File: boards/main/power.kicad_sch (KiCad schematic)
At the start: 20 parts, among them Q1 DMG3415U, U3 RT9080-33GJ5, U4 MCP73831T-2ACI_OT, U5 MAX17048G_T10

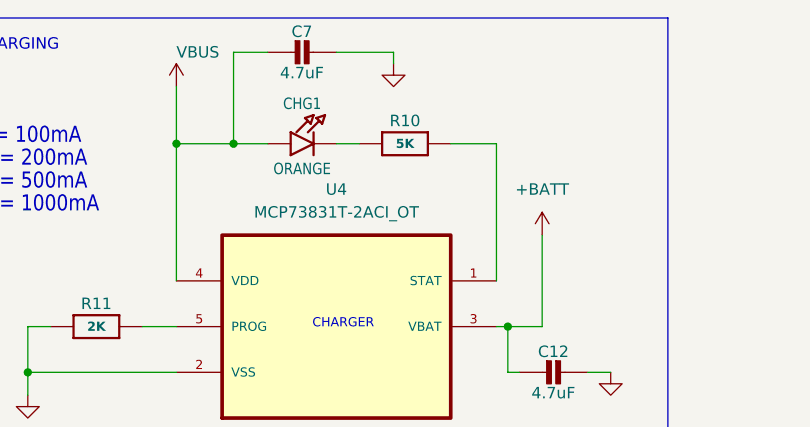
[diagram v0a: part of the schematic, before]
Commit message: Board migrations. Move to newer LED and IMU
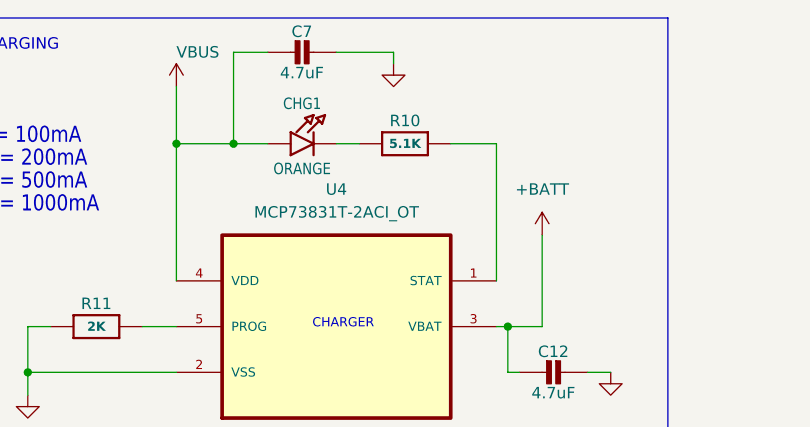
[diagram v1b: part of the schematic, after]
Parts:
- BATT1: DigiKey_PN (none) -> 455-S2B-PH-SM4-TBCT-ND; MPN S2B-PH-SM4-TB(LF)(SN) -> S2B-PH-SM4-TB; Manufacturer (none) -> JST Sales America Inc.
- C10, C14: Dielectric (none) -> X7R; DigiKey_PN (none) -> 1276-6844-1-ND; MPN 0402B104K160HI -> CL05B104KO5VPNC; Manufacturer (none) -> Samsung Electro-Mechanics; Voltage (none) -> 16V
- C11, C13, C8, C9: Dielectric (none) -> X5R; DigiKey_PN (none) -> 1276-6456-1-ND; Manufacturer (none) -> Samsung Electro-Mechanics; Voltage (none) -> 10V
- C12, C7: Dielectric (none) -> X5R; DigiKey_PN (none) -> 1276-1482-1-ND; MPN C0402X5R475M100NTC -> CL05A475MP5NRNC; Manufacturer (none) -> Samsung Electro-Mechanics; Voltage (none) -> 10V
- CHG1: DigiKey_PN (none) -> 160-1447-1-ND; Manufacturer (none) -> Lite-On Inc.; Sourcing_Note (none) -> Value field says ORANGE but LTST-C191KRKT is a RED 631nm LE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
- D1: DigiKey_PN (none) -> MBR0540TPMSCT-ND; MPN MBR0540 -> MBR0540-TP; Manufacturer (none) -> MCC (Micro Commercial Components)
- ONOFF1: DigiKey_PN (none) -> 455-1564-1-ND; Manufacturer (none) -> JST Sales America Inc.
- Q1: DigiKey_PN (none) -> DMG3415UDICT-ND; Manufacturer (none) -> Diodes Incorporated
- R10: value 5K -> 5.1K; DigiKey_PN (none) -> 311-5.10KHRCT-ND; MPN RT0603BRE075KL -> RC0603FR-075K1L; Manufacturer (none) -> YAGEO; Tolerance (none) -> 1%
- R11, R12, R9: Manufacturer (none) -> YAGEO; Tolerance (none) -> 1%
- U3: DigiKey_PN (none) -> 1028-1509-1-ND; Manufacturer (none) -> Richtek USA Inc.
- U4: DigiKey_PN (none) -> MCP73831T-2ACI/OTCT-ND; Manufacturer (none) -> Microchip Technology
- U5: DigiKey_PN (none) -> MAX17048G+T10CT-ND; Manufacturer (none) -> Analog Devices Inc./Maxim Integrated; Sourcing_Note (none) -> Operating range is -20C to +70C, the narrowest of any part 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
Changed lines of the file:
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@@
 			)
 		)
-		(property "MPN" "0402B104K160HI"
+		(property "MPN" "CL05B104KO5VPNC"
 			(at 86.36 101.6 90)
 			(hide yes)
@@
 			)
 		)
+    (property "Manufacturer" "Samsung Electro-Mechanics" (at 86.36 101.6 0)
+      (effects (font (size 1.27 1.27)) (hide yes))
+    )
+    (property "DigiKey_PN" "1276-6844-1-ND" (at 86.36 101.6 0)
+      (effects (font (size 1.27 1.27)) (hide yes))
+    )
+    (property "Voltage" "16V" (at 86.36 101.6 0)
+      (effects (font (size 1.27 1.27)) (hide yes))
+    )
+    (property "Dielectric" "X7R" (at 86.36 101.6 0)
+      (effects (font (size 1.27 1.27)) (hide yes))
+    )
 		(pin "1"
 		)
@@
 			)
 		)
+    (property "Manufacturer" "Diodes Incorporated" (at 163.83 48.26 0)
+      (effects (font (size 1.27 1.27)) (hide yes))
+    )
+    (property "DigiKey_PN" "DMG3415UDICT-ND" (at 163.83 48.26 0)
+      (effects (font (size 1.27 1.27)) (hide yes))
+    )
 		(pin "1"
 		)
@@
 			)
 		)
-		(property "Datasheet" "https://www.mouser.com/catalog/specsheets/JST_B4B_PH_SM4_TB_LF_SN_ePH.pdf"
+		(property "Datasheet" "https://www.jst-mfg.com/product/pdf/eng/eGH.pdf"
 			(at 203.2 41.91 0)
 			(hide yes)
@@
 			)
 		)
+    (property "Manufacturer" "JST Sales America Inc." (at 203.2 41.91 0)
+      (effects (font (size 1.27 1.27)) (hide yes))
+    )
+    (property "DigiKey_PN" "455-1564-1-ND" (at 203.2 41.91 0)
+      (effects (font (size 1.27 1.27)) (hide yes))
+    )
 		(pin "2"
 		)
@@
 			)
 		)
+    (property "Manufacturer" "YAGEO" (at 153.67 63.5 0)
+      (effects (font (size 1.27 1.27)) (hide yes))
+    )
+    (property "Tolerance" "1%" (at 153.67 63.5 0)
+      (effects (font (size 1.27 1.27)) (hide yes))
+    )
 		(pin "1"
 		)
@@
 			)
 		)
-		(property "Datasheet" "https://www.mouser.com/catalog/specsheets/JST_B4B_PH_SM4_TB_LF_SN_ePH.pdf"
+		(property "Datasheet" "https://www.jst-mfg.com/product/pdf/eng/ePH.pdf"
 			(at 224.79 41.91 0)
 			(hide yes)
@@
 			)
 		)
-		(property "MPN" "S2B-PH-SM4-TB(LF)(SN)"
+		(property "MPN" "S2B-PH-SM4-TB"
 			(at 224.79 41.91 0)
 			(hide yes)
@@
 			)
 		)
+    (property "Manufacturer" "JST Sales America Inc." (at 224.79 41.91 0)
+      (effects (font (size 1.27 1.27)) (hide yes))
+    )
+    (property "DigiKey_PN" "455-S2B-PH-SM4-TBCT-ND" (at 224.79 41.91 0)
+      (effects (font (size 1.27 1.27)) (hide yes))
+    )
 		(pin "2"
 		)
@@
 			)
 		)
-		(property "MPN" "C0402X5R475M100NTC"
+		(property "MPN" "CL05A475MP5NRNC"
 			(at 93.98 67.31 90)
 			(hide yes)
@@
 			)
 		)
+    (property "Manufacturer" "Samsung Electro-Mechanics" (at 93.98 67.31 0)
+      (effects (font (size 1.27 1.27)) (hide yes))
+    )
+    (property "DigiKey_PN" "1276-1482-1-ND" (at 93.98 67.31 0)
+      (effects (font (size 1.27 1.27)) (hide yes))
+    )
+    (property "Voltage" "10V" (at 93.98 67.31 0)
+      (effects (font (size 1.27 1.27)) (hide yes))
+    )
+    (property "Dielectric" "X5R" (at 93.98 67.31 0)
+      (effects (font (size 1.27 1.27)) (hide yes))
+    )
 		(pin "1"
 		)
@@
 			)
 		)
-		(property "MPN" "0402B104K160HI"
+		(property "MPN" "CL05B104KO5VPNC"
 			(at 207.01 66.04 90)
 			(hide yes)
@@
 			)
 		)
+    (property "Manufacturer" "Samsung Electro-Mechanics" (at 207.01 66.04 0)
+      (effects (font (size 1.27 1.27)) (hide yes))
+    )
+    (property "DigiKey_PN" "1276-6844-1-ND" (at 207.01 66.04 0)
+      (effects (font (size 1.27 1.27)) (hide yes))
+    )
+    (property "Voltage" "16V" (at 207.01 66.04 0)
+      (effects (font (size 1.27 1.27)) (hide yes))
+    )
+    (property "Dielectric" "X7R" (at 207.01 66.04 0)
+      (effects (font (size 1.27 1.27)) (hide yes))
+    )
 		(pin "1"
 		)
@@
 			)
 		)
+    (property "Manufacturer" "Lite-On Inc." (at 68.58 41.91 0)
+      (effects (font (size 1.27 1.27)) (hide yes))
+    )
+    (property "DigiKey_PN" "160-1447-1-ND" (at 68.58 41.91 0)
+      (effects (font (size 1.27 1.27)) (hide yes))
+    )
+    (property "Sourcing_Note" "Value field says ORANGE but LTST-C191KRKT is a RED 631nm LED. Pick one: keep this part and relabel the value, or substitute the orange member of the LTST-C191K family." (at 68.58 41.91 0)
+      (effects (font (size 1.27 1.27)) (hide yes))
+    )
 		(pin "2"
 		)
@@
 			)
 		)
+    (property "Manufacturer" "Samsung Electro-Mechanics" (at 236.22 64.77 0)
+      (effects (font (size 1.27 1.27)) (hide yes))
+    )
+    (property "DigiKey_PN" "1276-6456-1-ND" (at 236.22 64.77 0)
+      (effects (font (size 1.27 1.27)) (hide yes))
+    )
+    (property "Voltage" "10V" (at 236.22 64.77 0)
+      (effects (font (size 1.27 1.27)) (hide yes))
+    )
+    (property "Dielectric" "X5R" (at 236.22 64.77 0)
+      (effects (font (size 1.27 1.27)) (hide yes))
+    )
 		(pin "1"
 		)
@@
 			)
 		)
-		(property "MPN" "C0402X5R475M100NTC"
+		(property "MPN" "CL05A475MP5NRNC"
 			(at 66.04 31.75 90)
 			(hide yes)
@@
 			)
 		)
+    (property "Manufacturer" "Samsung Electro-Mechanics" (at 66.04 31.75 0)
+      (effects (font (size 1.27 1.27)) (hide yes))
+    )
+    (property "DigiKey_PN" "1276-1482-1-ND" (at 66.04 31.75 0)
+      (effects (font (size 1.27 1.27)) (hide yes))
+    )
+    (property "Voltage" "10V" (at 66.04 31.75 0)
+      (effects (font (size 1.27 1.27)) (hide yes))
+    )
+    (property "Dielectric" "X5R" (at 66.04 31.75 0)
+      (effects (font (size 1.27 1.27)) (hide yes))
+    )
 		(pin "1"
 		)
@@
 			)
 		)
+    (property "Manufacturer" "Analog Devices Inc./Maxim Integrated" (at 58.42 115.57 0)
+      (effects (font (size 1.27 1.27)) (hide yes))
+    )
+    (property "DigiKey_PN" "MAX17048G+T10CT-ND" (at 58.42 115.57 0)
+      (effects (font (size 1.27 1.27)) (hide yes))
+    )
+    (property "Sourcing_Note" "Operating range is -20C to +70C, the narrowest of any part on the board. Fine indoors, marginal for cold-weather hiking use." (at 58.42 115.57 0)
+      (effects (font (size 1.27 1.27)) (hide yes))
+    )
 		(pin "2"
 		)
@@
 			)
 		)
+    (property "Manufacturer" "YAGEO" (at 181.61 39.37 0)
+      (effects (font (size 1.27 1.27)) (hide yes))
+    )
+    (property "Tolerance" "1%" (at 181.61 39.37 0)
+      (effects (font (size 1.27 1.27)) (hide yes))
+    )
 		(pin "2"
 		)
@@
 			)
 		)
+    (property "Manufacturer" "Richtek USA Inc." (at 194.31 58.42 0)
+      (effects (font (size 1.27 1.27)) (hide yes))
+    )
+    (property "DigiKey_PN" "1028-1509-1-ND" (at 194.31 58.42 0)
+      (effects (font (size 1.27 1.27)) (hide yes))
+    )
 		(pin "5"
 		)
@@
 			)
 		)
+    (property "Manufacturer" "Samsung Electro-Mechanics" (at 214.63 66.04 0)
+      (effects (font (size 1.27 1.27)) (hide yes))
+    )
+    (property "DigiKey_PN" "1276-6456-1-ND" (at 214.63 66.04 0)
+      (effects (font (size 1.27 1.27)) (hide yes))
+    )
+    (property "Voltage" "10V" (at 214.63 66.04 0)
+      (effects (font (size 1.27 1.27)) (hide yes))
+    )
+    (property "Dielectric" "X5R" (at 214.63 66.04 0)
+      (effects (font (size 1.27 1.27)) (hide yes))
+    )
 		(pin "1"
 		)
@@
 			)
 		)
+    (property "Manufacturer" "Microchip Technology" (at 71.12 59.69 0)
+      (effects (font (size 1.27 1.27)) (hide yes))
+    )
+    (property "DigiKey_PN" "MCP73831T-2ACI/OTCT-ND" (at 71.12 59.69 0)
+      (effects (font (size 1.27 1.27)) (hide yes))
+    )
 		(pin "2"
 		)
@@
 			)
 		)
-		(property "Description" ""
+		(property "Description" "Schottky 40V 500mA SOD-123"
 			(at 158.75 55.88 0)
 			(hide yes)
@@
 			)
 		)
-		(property "MPN" "MBR0540"
+		(property "MPN" "MBR0540-TP"
 			(at 158.75 55.88 0)
 			(hide yes)
@@
 			)
 		)
+    (property "Manufacturer" "MCC (Micro Commercial Components)" (at 158.75 55.88 0)
+      (effects (font (size 1.27 1.27)) (hide yes))
+    )
+    (property "DigiKey_PN" "MBR0540TPMSCT-ND" (at 158.75 55.88 0)
+      (effects (font (size 1.27 1.27)) (hide yes))
+    )
 		(pin "1"
 		)
@@
 			)
 		)
-		(property "Description" ""
+		(property "Description" "MCP73831 PROG resistor - sets charge current"
 			(at 44.45 62.23 0)
 			(hide yes)
@@
 			)
 		)
+    (property "Manufacturer" "YAGEO" (at 44.45 62.23 0)
+      (effects (font (size 1.27 1.27)) (hide yes))
+    )
+    (property "Tolerance" "1%" (at 44.45 62.23 0)
+      (effects (font (size 1.27 1.27)) (hide yes))
+    )
 		(pin "1"
 		)
@@
 			)
 		)
+    (property "Manufacturer" "Samsung Electro-Mechanics" (at 172.72 66.04 0)
+      (effects (font (size 1.27 1.27)) (hide yes))
+    )
+    (property "DigiKey_PN" "1276-6456-1-ND" (at 172.72 66.04 0)
+      (effects (font (size 1.27 1.27)) (hide yes))
+    )
+    (property "Voltage" "10V" (at 172.72 66.04 0)
+      (effects (font (size 1.27 1.27)) (hide yes))
+    )
+    (property "Dielectric" "X5R" (at 172.72 66.04 0)
+      (effects (font (size 1.27 1.27)) (hide yes))
+    )
 		(pin "1"
 		)
@@
 			)
 		)
-		(property "Value" "5K"
+		(property "Value" "5.1K"
 			(at 78.74 41.91 0)
 			(show_name no)
@@
 			)
 		)
-		(property "MPN" "RT0603BRE075KL"
+		(property "MPN" "RC0603FR-075K1L"
 			(at 78.74 41.91 0)
 			(hide yes)
@@
 			)
 		)
+    (property "Manufacturer" "YAGEO" (at 78.74 41.91 0)
+      (effects (font (size 1.27 1.27)) (hide yes))
+    )
+    (property "DigiKey_PN" "311-5.10KHRCT-ND" (at 78.74 41.91 0)
+      (effects (font (size 1.27 1.27)) (hide yes))
+    )
+    (property "Tolerance" "1%" (at 78.74 41.91 0)
+      (effects (font (size 1.27 1.27)) (hide yes))
+    )
 		(pin "1"
 		)
@@
 			)
 		)
+    (property "Manufacturer" "Samsung Electro-Mechanics" (at 236.22 74.93 0)
+      (effects (font (size 1.27 1.27)) (hide yes))
+    )
+    (property "DigiKey_PN" "1276-6456-1-ND" (at 236.22 74.93 0)
+      (effects (font (size 1.27 1.27)) (hide yes))
+    )
+    (property "Voltage" "10V" (at 236.22 74.93 0)
+      (effects (font (size 1.27 1.27)) (hide yes))
+    )
+    (property "Dielectric" "X5R" (at 236.22 74.93 0)
+      (effects (font (size 1.27 1.27)) (hide yes))
+    )
 		(pin "2"
 		)

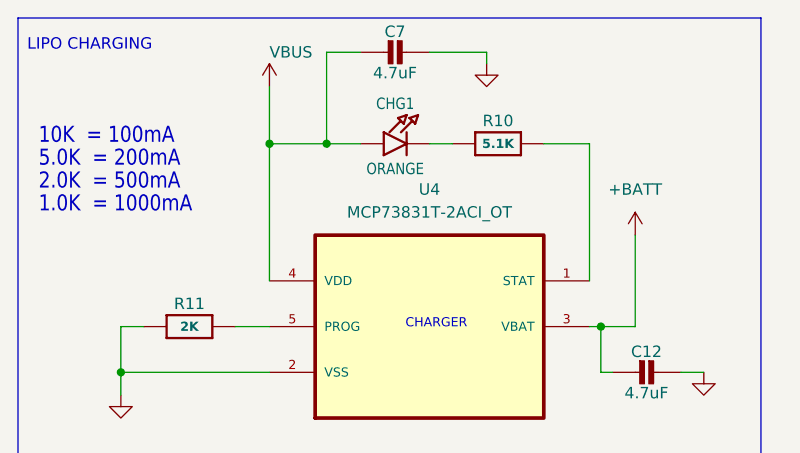
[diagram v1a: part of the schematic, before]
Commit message: some more component reworking. Moved to 10 lane ribbon connects between all boards
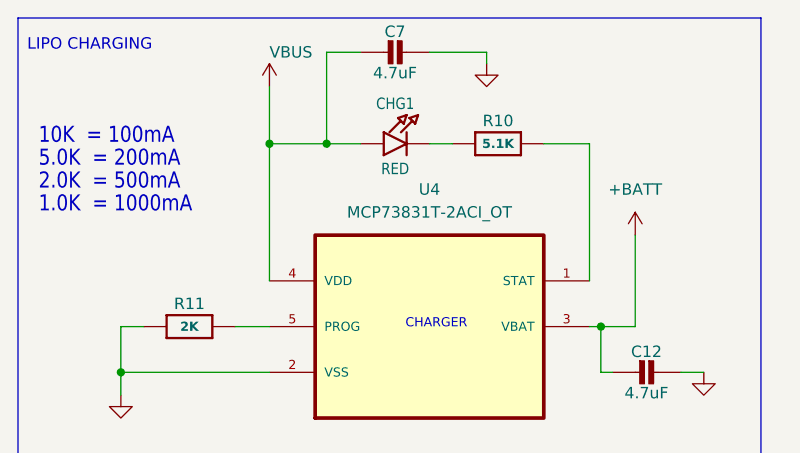
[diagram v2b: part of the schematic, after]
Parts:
- BATT1: symbol S2B-PH-SM4-TB_LF__SN_:S2B-PH-SM4-TB_LF__SN_ -> smart_compass_main:S2B-PH-SM4-TB_LF__SN_
- C10, C11, C13, C8, C9: symbol Adafruit ESP32-S3 8MB No PSRAM-eagle-import:CAP_CERAMIC0805-NOOUTLINE -> smart_compass_main:CAP_CERAMIC0805-NOOUTLINE
- C12, C14, C7: symbol Adafruit ESP32-S3 8MB No PSRAM-eagle-import:CAP_CERAMIC0603_NO -> smart_compass_main:CAP_CERAMIC0603_NO
- CHG1: value ORANGE -> RED; symbol Adafruit ESP32-S3 8MB No PSRAM-eagle-import:LED0603_NOOUTLINE -> smart_compass_main:LED0603_NOOUTLINE; Sourcing_Note Value field says ORANGE but LTST-C191KRKT is a RED 631nm LE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 -> Value relabelled ORANGE -> RED to agree with the MPN. LTST-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
- D1: symbol Adafruit ESP32-S3 8MB No PSRAM-eagle-import:DIODE-SCHOTTKYSOD-123 -> smart_compass_main:DIODE-SCHOTTKYSOD-123
- ONOFF1: symbol SM02B-GHS-TB:SM02B-GHS-TB -> smart_compass_main:SM02B-GHS-TB
- Q1: symbol Adafruit ESP32-S3 8MB No PSRAM-eagle-import:MOSFET-P -> smart_compass_main:MOSFET-P
- R10, R11, R12, R9: symbol Adafruit ESP32-S3 8MB No PSRAM-eagle-import:RESISTOR_0603_NOOUT -> smart_compass_main:RESISTOR_0603_NOOUT
- U3: symbol Adafruit ESP32-S3 8MB No PSRAM-eagle-import:VREG_SOT23-5 -> smart_compass_main:VREG_SOT23-5
- U4: symbol MCP73831T-2ACI_OT:MCP73831T-2ACI_OT -> smart_compass_main:MCP73831T-2ACI_OT
- U5: symbol MAX17048G_T10:MAX17048G_T10 -> smart_compass_main:MAX17048G_T10

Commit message: Add a voltage booster and logic shift to the LED ring. Power consumption implications, but necessary
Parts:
- BATT1: footprint S2B-PH-SM4-TB_LF__SN_:JST_S2B-PH-SM4-TB_LF__SN_ -> (none)
- ONOFF1: footprint SM02B-GHS-TB:JST_SM02B-GHS-TB -> (none)
- Q1: footprint DMG3415U-7:SOT95P240X105-3N -> (none)
- U3: footprint RT9080-33GJ5:SOT94P280X100-5N -> (none)
- U4: footprint MCP73831T-2ACI_OT:SOT95P280X145-5N -> (none)
- U5: footprint MAX17048G_T10:SON50P200X200X80-9N -> (none)
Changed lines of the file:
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@@
 			)
 		)
-		(property "Footprint" "DMG3415U-7:SOT95P240X105-3N"
+		(property "Footprint" ""
 			(at 163.83 48.26 0)
 			(hide yes)
@@
 			)
 		)
-		(property "Footprint" "SM02B-GHS-TB:JST_SM02B-GHS-TB"
+		(property "Footprint" ""
 			(at 203.2 41.91 0)
 			(hide yes)
@@
 			)
 		)
-		(property "Footprint" "S2B-PH-SM4-TB_LF__SN_:JST_S2B-PH-SM4-TB_LF__SN_"
+		(property "Footprint" ""
 			(at 224.79 41.91 0)
 			(hide yes)
@@
 			)
 		)
-		(property "Footprint" "MAX17048G_T10:SON50P200X200X80-9N"
+		(property "Footprint" ""
 			(at 58.42 115.57 0)
 			(hide yes)
@@
 			)
 		)
-		(property "Footprint" "RT9080-33GJ5:SOT94P280X100-5N"
+		(property "Footprint" ""
 			(at 194.31 58.42 0)
 			(hide yes)
@@
 			)
 		)
-		(property "Footprint" "MCP73831T-2ACI_OT:SOT95P280X145-5N"
+		(property "Footprint" ""
 			(at 71.12 59.69 0)
 			(hide yes)

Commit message: Going down the todo list. Slowed the charge speed
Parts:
- removed C10: 0.1uF, Capacitor_SMD:C_0402_1005Metric, symbol smart_compass_main:CAP_CERAMIC0805-NOOUTLINE
- R11: value 2K -> 3.9K; MPN RC0603FR-072KL -> RC0603FR-073K9L
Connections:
- no-connect marks 0 -> 1
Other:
- note added: "3.9K = 256mA"
- note removed: "2.0K = 500mA"

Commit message: Update the footprint for the flash chip
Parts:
- renumbered C11 to C10, C12 to C11, C13 to C12, C14 to C13
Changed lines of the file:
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@@
 		(in_pos_files yes)
 		(dnp no)
-		(property "Reference" "C14"
+		(property "Reference" "C13"
 			(at 84.07 100.35 90)
 			(show_name no)
@@
 			(project "SmartCompass"
 				(path "/0c161f28-8075-4403-a867-35208f463636/44fc6246-5945-463a-870f-e1f278c176e3"
-					(reference "C14")
+					(reference "C13")
 					(unit 1)
 				)
@@
 		(dnp no)
 		(fields_autoplaced yes)
-		(property "Reference" "#PWR039"
+		(property "Reference" "#PWR038"
 			(at 74.93 99.06 0)
 			(hide yes)
@@
 			(project "SmartCompass"
 				(path "/0c161f28-8075-4403-a867-35208f463636/44fc6246-5945-463a-870f-e1f278c176e3"
-					(reference "#PWR039")
+					(reference "#PWR038")
 					(unit 1)
 				)
@@
 		(in_pos_files yes)
 		(dnp no)
-		(property "Reference" "C12"
+		(property "Reference" "C11"
 			(at 95.23 65.02 90)
 			(show_name no)
@@
 			(project "SmartCompass"
 				(path "/0c161f28-8075-4403-a867-35208f463636/44fc6246-5945-463a-870f-e1f278c176e3"
-					(reference "C12")
+					(reference "C11")
 					(unit 1)
 				)
@@
 		(dnp no)
 		(fields_autoplaced yes)
-		(property "Reference" "#PWR040"
+		(property "Reference" "#PWR039"
 			(at 93.98 104.14 0)
 			(hide yes)
@@
 			(project "SmartCompass"
 				(path "/0c161f28-8075-4403-a867-35208f463636/44fc6246-5945-463a-870f-e1f278c176e3"
-					(reference "#PWR040")
+					(reference "#PWR039")
 					(unit 1)
 				)
@@
 		(dnp no)
 		(fields_autoplaced yes)
-		(property "Reference" "#PWR042"
+		(property "Reference" "#PWR041"
 			(at 88.9 135.89 0)
 			(hide yes)
@@
 			(project "SmartCompass"
 				(path "/0c161f28-8075-4403-a867-35208f463636/44fc6246-5945-463a-870f-e1f278c176e3"
-					(reference "#PWR042")
+					(reference "#PWR041")
 					(unit 1)
 				)
@@
 		(dnp no)
 		(fields_autoplaced yes)
-		(property "Reference" "#PWR041"
+		(property "Reference" "#PWR040"
 			(at 30.48 124.46 0)
 			(hide yes)
@@
 			(project "SmartCompass"
 				(path "/0c161f28-8075-4403-a867-35208f463636/44fc6246-5945-463a-870f-e1f278c176e3"
-					(reference "#PWR041")
+					(reference "#PWR040")
 					(unit 1)
 				)
@@
 		(dnp no)
 		(fields_autoplaced yes)
-		(property "Reference" "#PWR038"
+		(property "Reference" "#PWR037"
 			(at 243.84 81.28 0)
 			(hide yes)
@@
 			(project "SmartCompass"
 				(path "/0c161f28-8075-4403-a867-35208f463636/44fc6246-5945-463a-870f-e1f278c176e3"
-					(reference "#PWR038")
+					(reference "#PWR037")
 					(unit 1)
 				)
@@
 		(dnp no)
 		(fields_autoplaced yes)
-		(property "Reference" "#PWR037"
+		(property "Reference" "#PWR036"
 			(at 214.63 77.47 0)
 			(hide yes)
@@
 			(project "SmartCompass"
 				(path "/0c161f28-8075-4403-a867-35208f463636/44fc6246-5945-463a-870f-e1f278c176e3"
-					(reference "#PWR037")
+					(reference "#PWR036")
 					(unit 1)
 				)
@@
 		(in_pos_files yes)
 		(dnp no)
-		(property "Reference" "C11"
+		(property "Reference" "C10"
 			(at 212.34 64.79 90)
 			(show_name no)
@@
 			(project "SmartCompass"
 				(path "/0c161f28-8075-4403-a867-35208f463636/44fc6246-5945-463a-870f-e1f278c176e3"
-					(reference "C11")
+					(reference "C10")
 					(unit 1)
 				)
@@
 		(in_pos_files yes)
 		(dnp no)
-		(property "Reference" "C13"
+		(property "Reference" "C12"
 			(at 234.97 77.22 90)
 			(show_name no)
@@
 			(project "SmartCompass"
 				(path "/0c161f28-8075-4403-a867-35208f463636/44fc6246-5945-463a-870f-e1f278c176e3"
-					(reference "C13")
+					(reference "C12")
 					(unit 1)
 				)
